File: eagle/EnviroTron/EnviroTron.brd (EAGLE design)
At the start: 27.1 x 35.6 mm, 29 parts

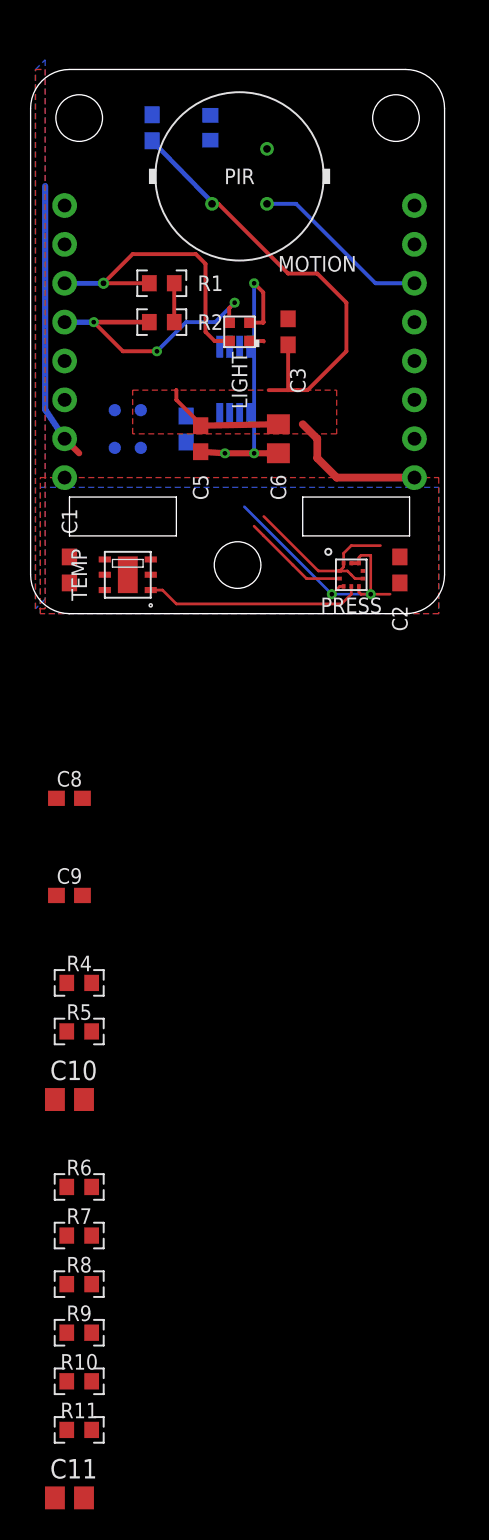
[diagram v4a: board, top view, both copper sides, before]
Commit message: Completed initial routing of all signals for new board layout.
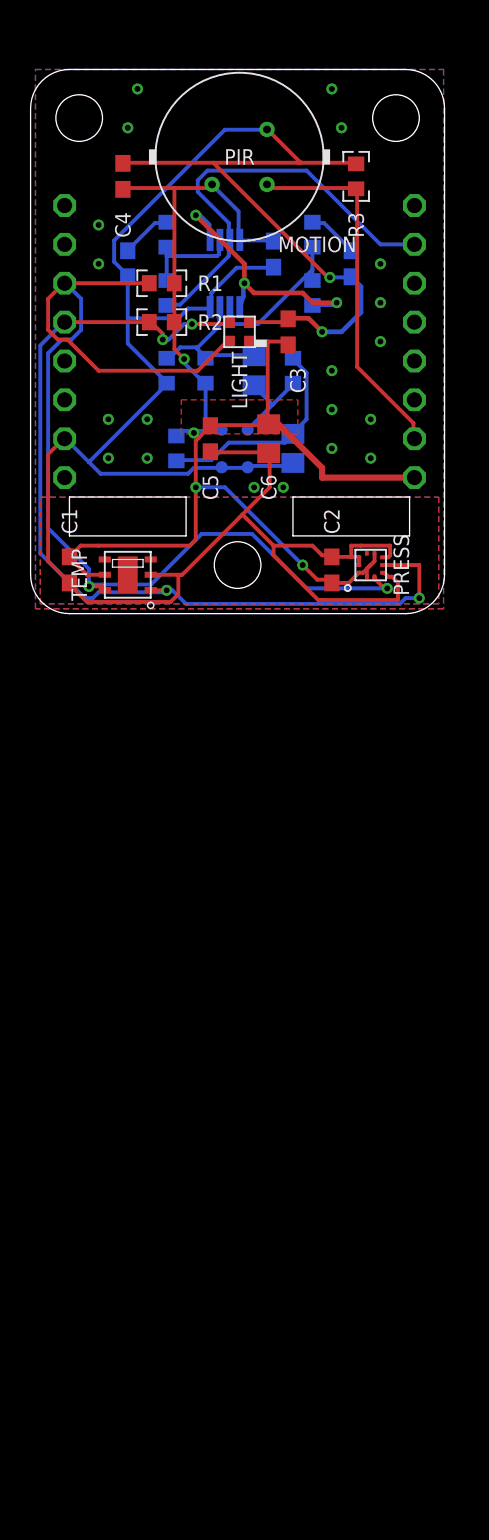
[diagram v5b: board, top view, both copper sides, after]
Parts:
- moved R11 78.3 mm to (8.89, 24.8), flipped to the bottom, turned to 90 degrees
- moved C11 74.6 mm to (14.6, 15.9), flipped to the bottom, turned to 90 degrees
- moved R9 73.4 mm to (18.4, 24.8), flipped to the bottom, turned to 90 degrees
- moved R10 71.3 mm to (8.89, 21.0), flipped to the bottom, turned to 90 degrees
- moved R8 66.5 mm to (18.4, 21.0), flipped to the bottom, turned to 90 degrees
- moved R7 56.8 mm to (8.89, 15.9), flipped to the bottom, turned to 270 degrees
- moved R6 54.0 mm to (11.4, 15.9), flipped to the bottom, turned to 90 degrees
- moved C10 45.0 mm to (17.1, 10.8), flipped to the bottom, turned to 270 degrees
- moved R4 42.4 mm to (17.1, 15.9), flipped to the bottom, turned to 270 degrees
- moved C9 41.5 mm to (6.35, 22.9), flipped to the bottom, turned to 270 degrees
- moved C8 39.5 mm to (21.0, 22.9), flipped to the bottom, turned to 270 degrees
- moved R5 38.6 mm to (9.53, 10.8), flipped to the bottom, turned to 270 degrees
- moved C7 12.8 mm to (15.9, 23.5)
- moved R3 10.0 mm to (21.3, 28.6), flipped to the top
- moved SOUND 7.10 mm to (13.3, 10.8)
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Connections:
- removed net N$11: C8.2, C9.2
- removed net N$3: C5.1, C6.1
- removed net N$4: C5.2, C6.2
- net 3V3: now also C5.1, C6.1, U$1.8
- net GND: now also C5.2, C6.2, C8.2, C9.2, U$1.4
- net PIROUT: now also COMMS.D8; no longer COMMS.D0
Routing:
- net GND: track 51.4 -> 162.2 mm, vias 4 -> 22
- net SCL: track 29.0 -> 70.4 mm, vias 1 -> 2
- net 3V3: track 56.9 -> 92.3 mm, vias 0 -> 4
- net AMP-OUT: track 0.00 -> 27.7 mm
- net SDA: track 34.5 -> 60.2 mm, vias 3 -> 4
- net N$2: track 0.00 -> 17.8 mm, vias 0 -> 3
- net N$5: track 0.00 -> 14.1 mm
- net PIROUT: track 12.1 -> 23.9 mm
- net MIC-OUT: track 0.00 -> 9.97 mm
- net N$6: track 0.00 -> 9.96 mm
- net N$9: track 0.00 -> 6.62 mm
- net N$8: track 0.00 -> 6.04 mm
- net N$4: track 5.09 -> 0.00 mm, vias 1 -> 0
- net N$3: track 5.08 -> 0.00 mm
- net N$10: track 0.00 -> 3.37 mm
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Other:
- outline, holes or cut-outs redrawn
